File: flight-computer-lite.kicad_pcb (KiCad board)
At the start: 2 copper layers, 65 x 65 mm, 8 parts, among them J1 USB_C_Receptacle_USB2.0_16P, J2 Micro_SD_Card_Det2, U1 MS5611-01BA, U2 BME680, U3 LIS3MDL, U4 RP2040, U5 W25Q32JVZP

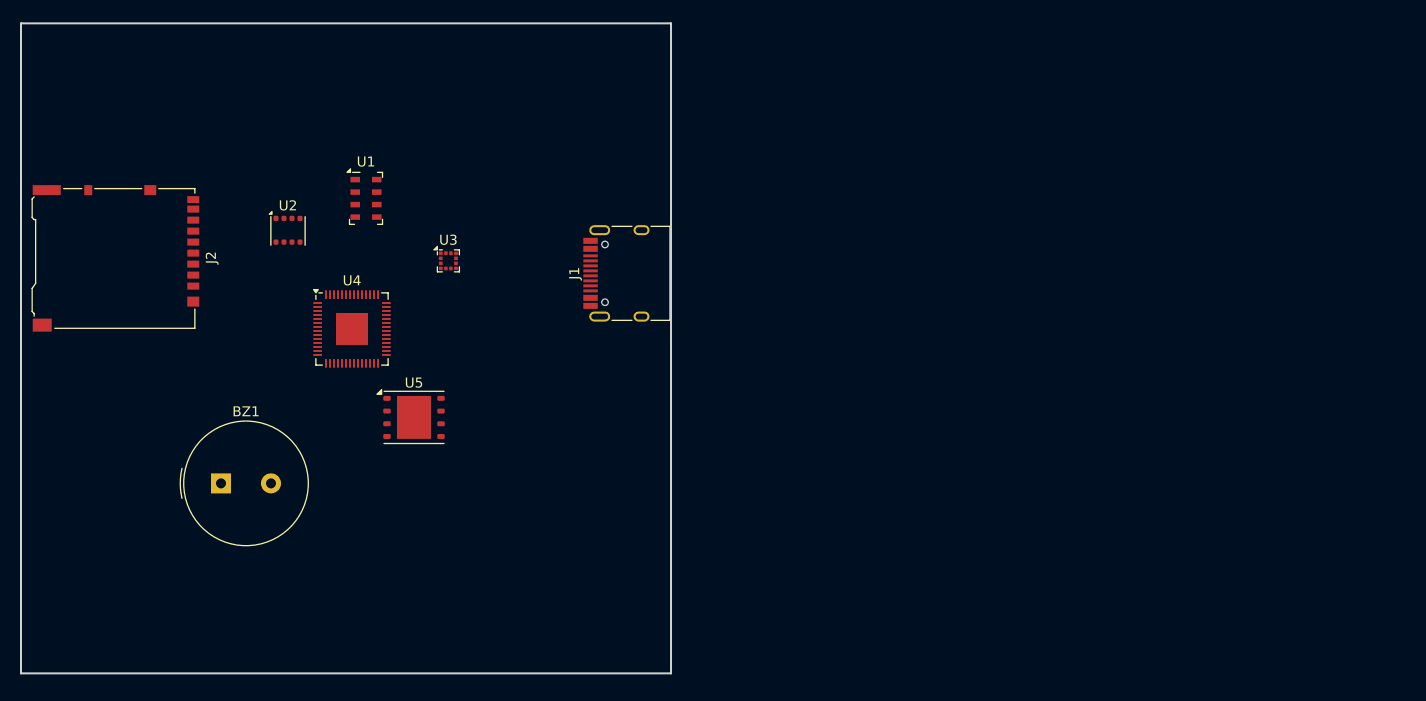
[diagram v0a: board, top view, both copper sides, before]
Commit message: Added mounting holes
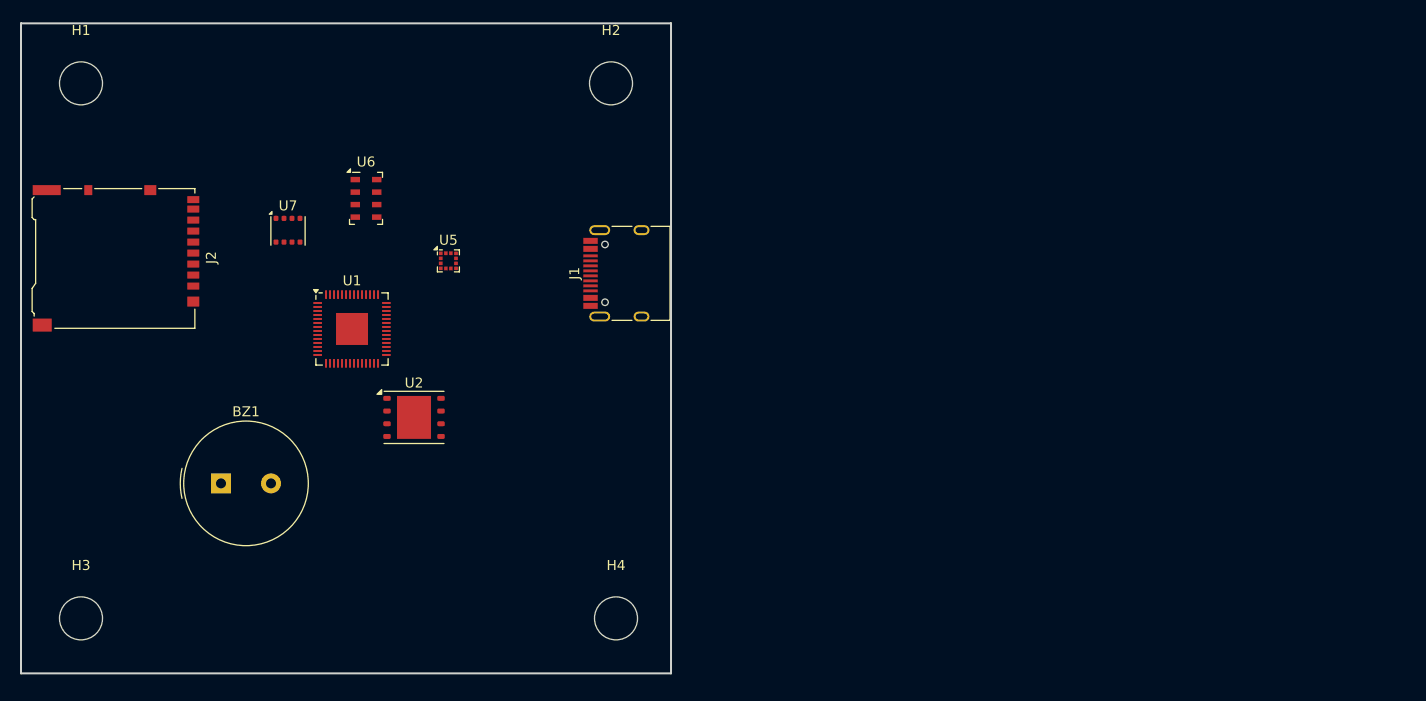
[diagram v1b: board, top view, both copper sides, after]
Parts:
- added H1: MountingHole, MountingHole:MountingHole_4.3mm_M4, F.Cu at (121.0, 60.5)
- added H2: MountingHole, MountingHole:MountingHole_4.3mm_M4, F.Cu at (174.0, 60.5)
- added H3: MountingHole, MountingHole:MountingHole_4.3mm_M4, F.Cu at (121.0, 114.0)
- added H4: MountingHole, MountingHole:MountingHole_4.3mm_M4, F.Cu at (174.5, 114.0)
- renumbered U4 to U1, U5 to U2, U3 to U5, U1 to U6, U2 to U7

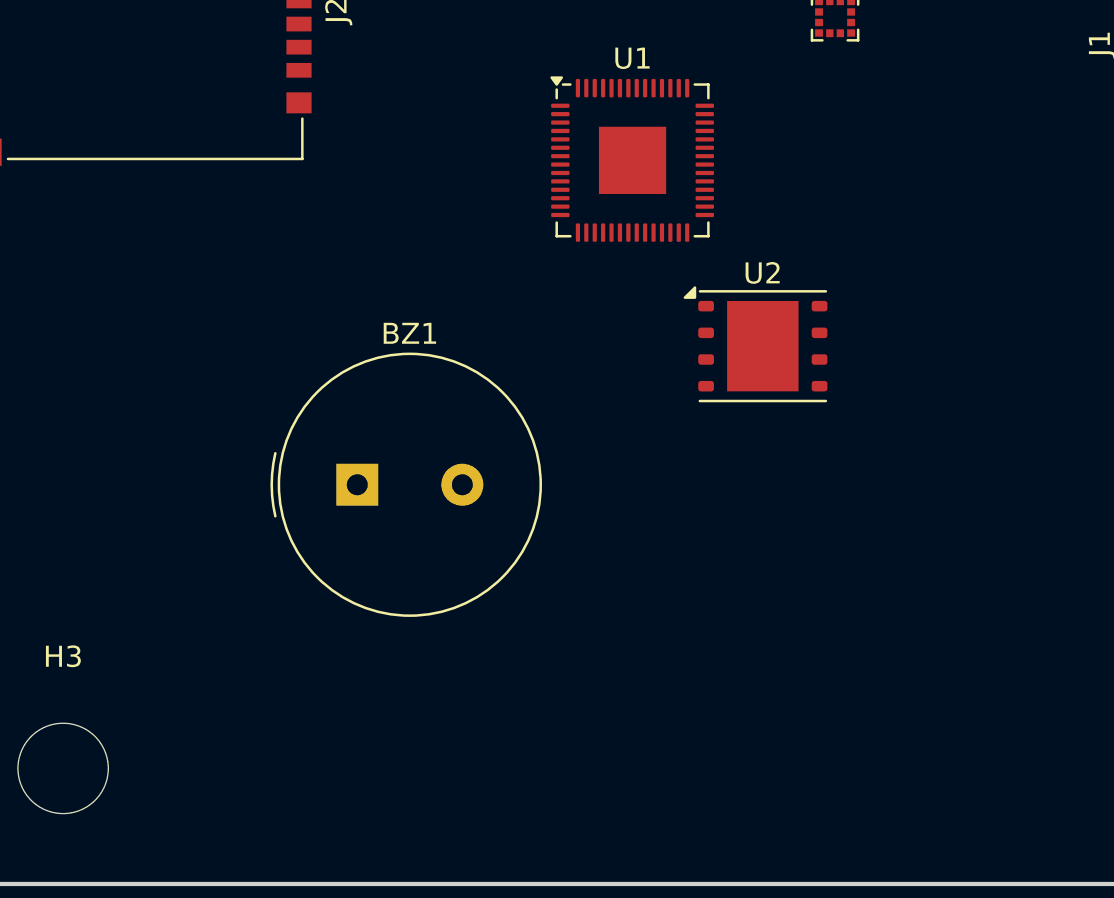
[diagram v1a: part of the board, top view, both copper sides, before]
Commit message: Changed board surface finish, added GPS
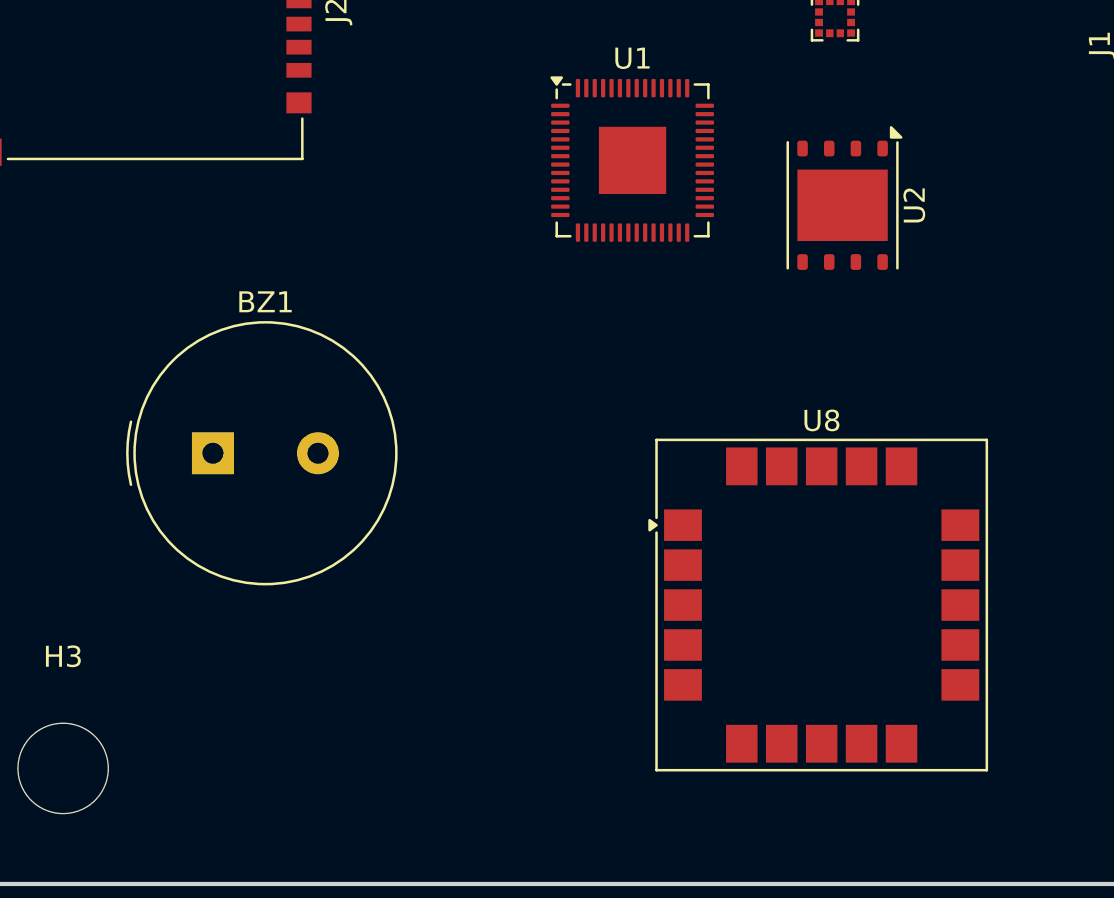
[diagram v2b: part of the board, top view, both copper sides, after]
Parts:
- added U8: SAM-M8Q, RF_GPS:ublox_SAM-M8Q, F.Cu at (157.1, 106.2)
- moved U2 7.70 mm to (158.1, 87.2), turned to -90 degrees
- moved BZ1 7.03 mm to (128.1, 99.0)

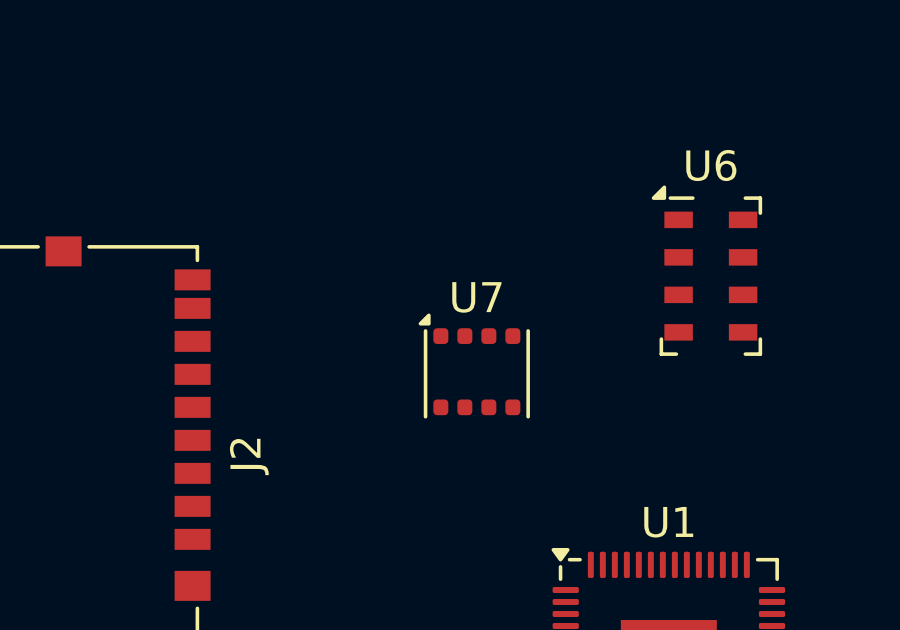
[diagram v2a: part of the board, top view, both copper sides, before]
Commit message: replaced nrnd BME680 with HDC2080
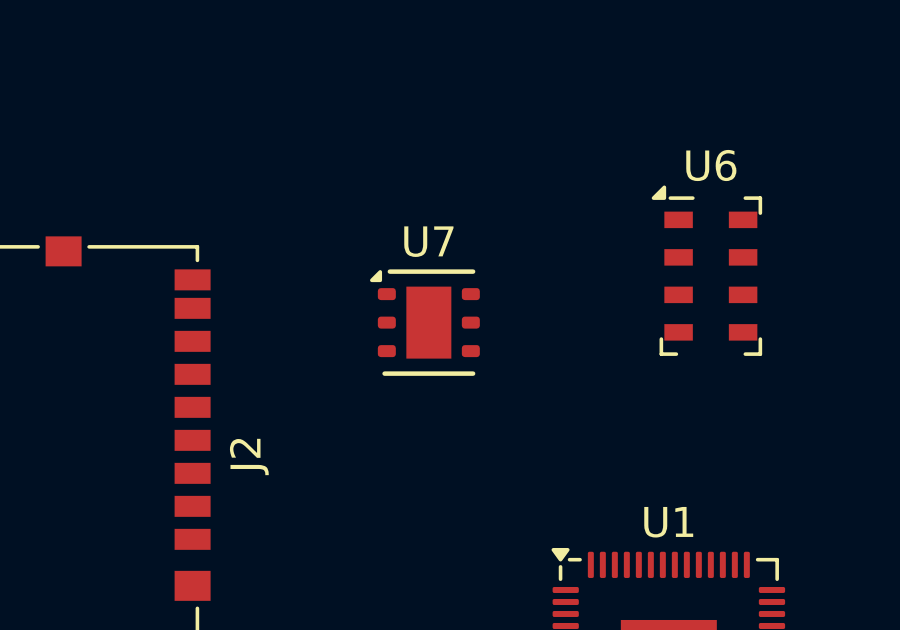
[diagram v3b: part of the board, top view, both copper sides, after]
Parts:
- U7: value BME680 -> HDC2080; footprint Package_LGA:Bosch_LGA-8_3x3mm_P0.8mm_ClockwisePinNumbering -> Package_SON:Texas_PWSON-N6
- moved U7 2.29 mm to (140.1, 73.5)
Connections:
- U7 pad 2: unconnected-(U7-CSB-Pad2) -> GND
- U7 pad 5: unconnected-(U7-SDO-Pad5) -> +1V8

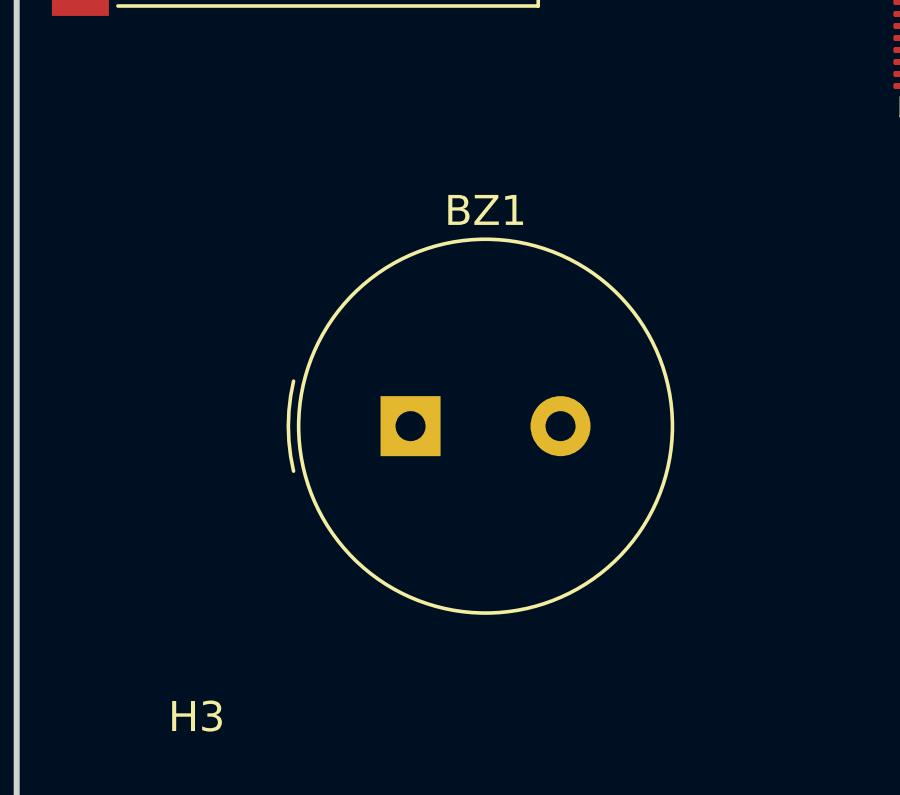
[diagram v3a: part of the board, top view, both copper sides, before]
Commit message: Changed buzzer partno
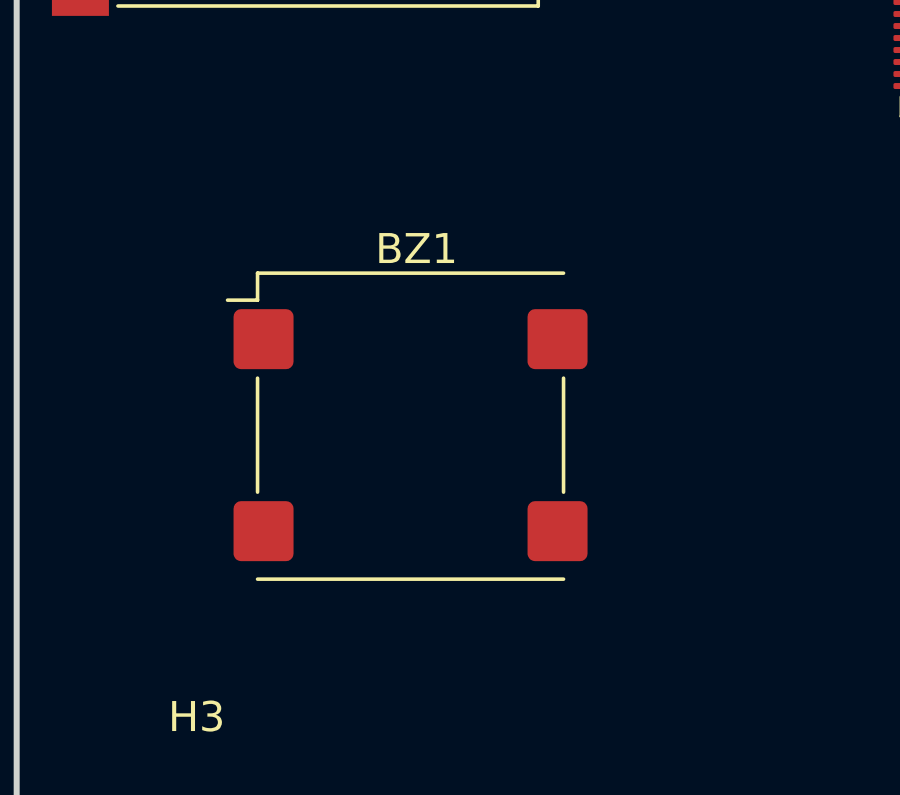
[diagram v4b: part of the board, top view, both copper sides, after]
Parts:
- BZ1: footprint Buzzer_Beeper:Buzzer_TDK_PS1240P02BT_D12.2mm_H6.5mm -> Buzzer_Beeper:MagneticBuzzer_PUI_SMT-1028-T-2-R

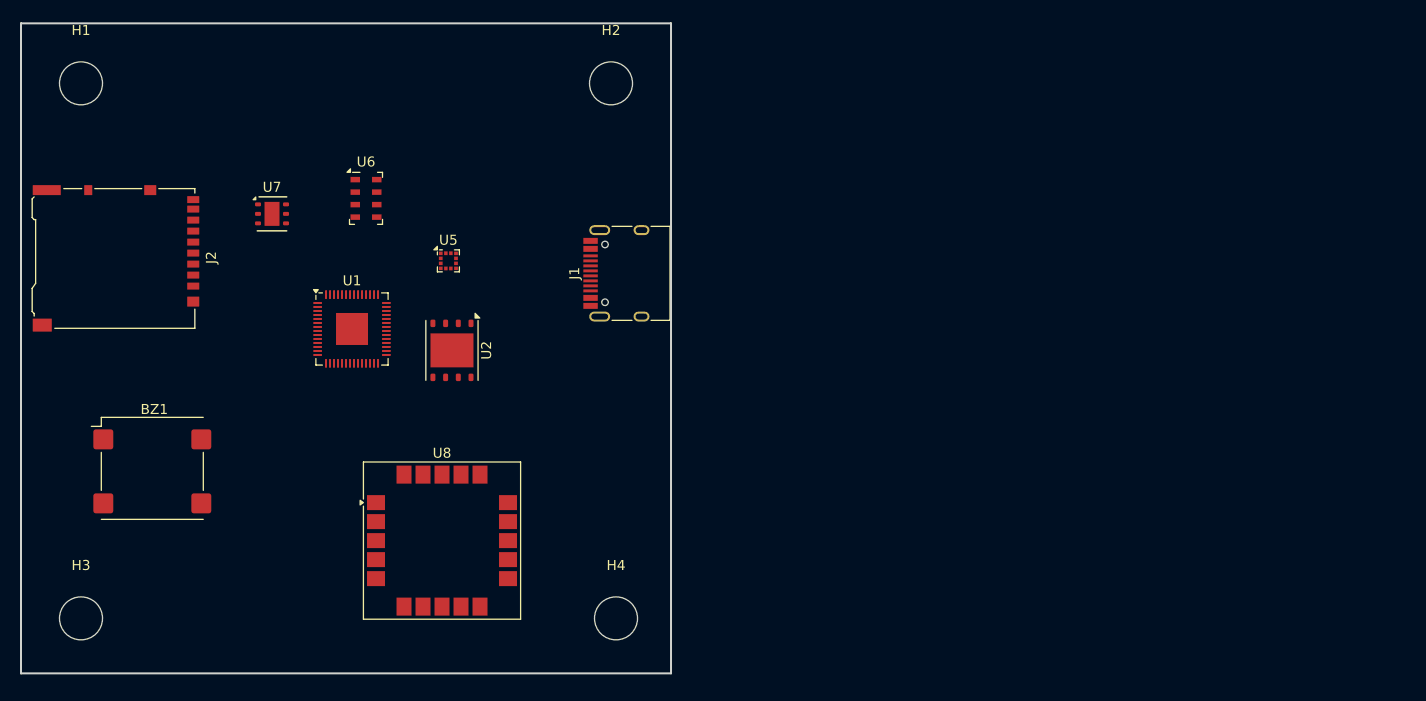
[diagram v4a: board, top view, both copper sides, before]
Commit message: Created LRI_partlib
Created a local part library for the project (that can be reused on others in the future).
Added the ICM-42688-P and BMI088 IMUs to it.
Added them to the PCB and reorganized some things.
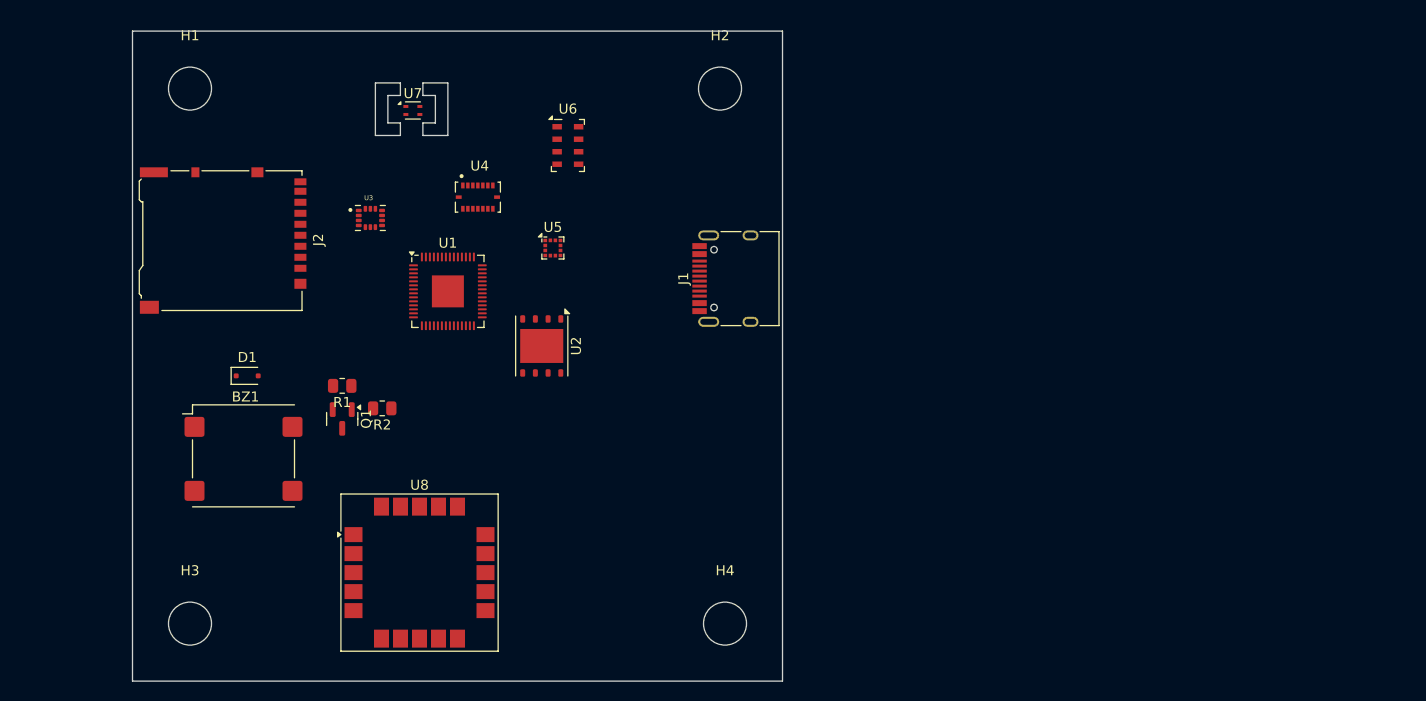
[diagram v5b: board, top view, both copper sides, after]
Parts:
- added D1: 1N4148W, Diode_SMD:D_SOD-323F, F.Cu at (137.6, 89.8)
- added Q1: BSS138, Package_TO_SOT_SMD:SOT-23, F.Cu at (147.1, 94.1)
- added R1: 100K, Resistor_SMD:R_0805_2012Metric, F.Cu at (147.1, 90.8)
- added R2: 100, Resistor_SMD:R_0805_2012Metric, F.Cu at (151.1, 93.0)
- added U3: ICM-42688-P, LRI_partlib:PQFN50P300X250X97-14N, F.Cu at (149.9, 74.0)
- added U4: BMI088, LRI_partlib:PQFN50P450X300X100-16N, F.Cu at (160.7, 71.9)
- U7: value HDC2080 -> SHT4x; footprint Package_SON:Texas_PWSON-N6 -> Sensor_Humidity:Sensirion_DFN-4_1.5x1.5mm_P0.8mm_SHT4x_NoCentralPad
- moved U6 20.9 mm to (169.7, 66.7)
- moved U7 17.5 mm to (154.2, 63.2)
- moved H1 10.9 mm to (131.9, 61.0)
- moved H2 10.9 mm to (184.9, 61.0)
- moved H3 10.9 mm to (131.9, 114.5)
- moved H4 10.9 mm to (185.4, 114.5)
- moved J1 10.9 mm to (186.9, 80.0)
- moved J2 10.9 mm to (135.2, 76.2)
- moved U5 10.5 mm to (168.2, 77.0)
- moved U1 10.3 mm to (157.7, 81.3)
- moved BZ1 9.21 mm to (137.2, 97.8)
- moved U2 8.99 mm to (167.1, 86.8)
- moved U8 3.91 mm to (154.8, 109.4)
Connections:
- BZ1 pad 1: unconnected-(BZ1-+-Pad1) -> +3V3
- BZ1 pad 2: unconnected-(BZ1---Pad2) -> Net-(BZ1--)
- J1 pad A1: Net-(J1-GND-PadA1) -> GND
- J1 pad A12: Net-(J1-GND-PadA1) -> GND
- J1 pad B1: Net-(J1-GND-PadA1) -> GND
- J1 pad B12: Net-(J1-GND-PadA1) -> GND
- U1 pad 57: unconnected-(U1-GND-Pad57) -> GND
- U2 pad 4: unconnected-(U2-GND-Pad4) -> GND
- U5 pad 12: Net-(U5-GND-Pad12) -> GND
- U5 pad 2: Net-(U5-GND-Pad12) -> GND
- U5 pad 3: Net-(U5-GND-Pad12) -> GND
- U6 pad 3: unconnected-(U6-GND-Pad3) -> GND
- U7 pad 2: GND -> unconnected-(U7-SCL-Pad2)
- U8 pad 1: Net-(U8-GND-Pad1) -> GND
- U8 pad 10: Net-(U8-GND-Pad1) -> GND
- U8 pad 11: Net-(U8-GND-Pad1) -> GND
- U8 pad 15: Net-(U8-GND-Pad1) -> GND
- U8 pad 16: Net-(U8-GND-Pad1) -> GND
- U8 pad 20: Net-(U8-GND-Pad1) -> GND
- U8 pad 4: Net-(U8-GND-Pad1) -> GND
- U8 pad 5: Net-(U8-GND-Pad1) -> GND
- U8 pad 6: Net-(U8-GND-Pad1) -> GND
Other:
- outline, holes or cut-outs redrawn
- board text added: "Ali Albaghdadi Brent Schaaf Jacob Baumel"
- board text added: "Flight Computer Lite rev.A {dblquote}Digital Tripper{dblquote}"
